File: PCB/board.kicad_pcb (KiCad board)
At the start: 2 copper layers, 161 parts, among them J1 Micro_SD_Card, J10 Conn_01x10, J11 Conn_01x02, J12 Conn_02x04_Odd_Even, J13 Conn_01x02, J14 Conn_01x02, J15 Conn_01x03, J16 Conn_01x02, J17 Conn_01x05, J18 Conn_01x04, J19 Conn_01x04, J2 Conn_ARM_JTAG_SWD_10, J20 Conn_01x02, J21 Conn_01x03, J22 Conn_02x04_Odd_Even, J23 Conn_01x04, J24 Conn_01x04, J25 Conn_01x02, J26 Conn_01x03, J27 Conn_02x04_Odd_Even, J28 Conn_01x04, J29 Conn_01x04, J3 USB_C_Receptacle_USB2.0_14P, J30 Conn_01x02, J31 Conn_01x03, J32 Conn_01x02, J33 Conn_01x02, J34 Conn_01x02, J35 Conn_01x02, J36 Conn_01x02, J37 Conn_01x02, J4 Conn_01x04, J5 Conn_01x04, J6 Conn_01x02, J7 Conn_01x03, J8 Conn_02x04_Odd_Even, J9 Conn_01x10, Q1 IRLML6402, Q2 NMOS, Q3 NMOS, Q4 NMOS, Q5 STP55NF06L, Q6 STP55NF06L, SW1 SW_Push, SW2 SW_Push, U1 STM32H743VITx, U2 AP7361C, U4 TMC Stepstick, U5 TMC Stepstick, U6 TMC Stepstick, U7 TMC Stepstick, U8 AP63203WU, Y2 25 MHz

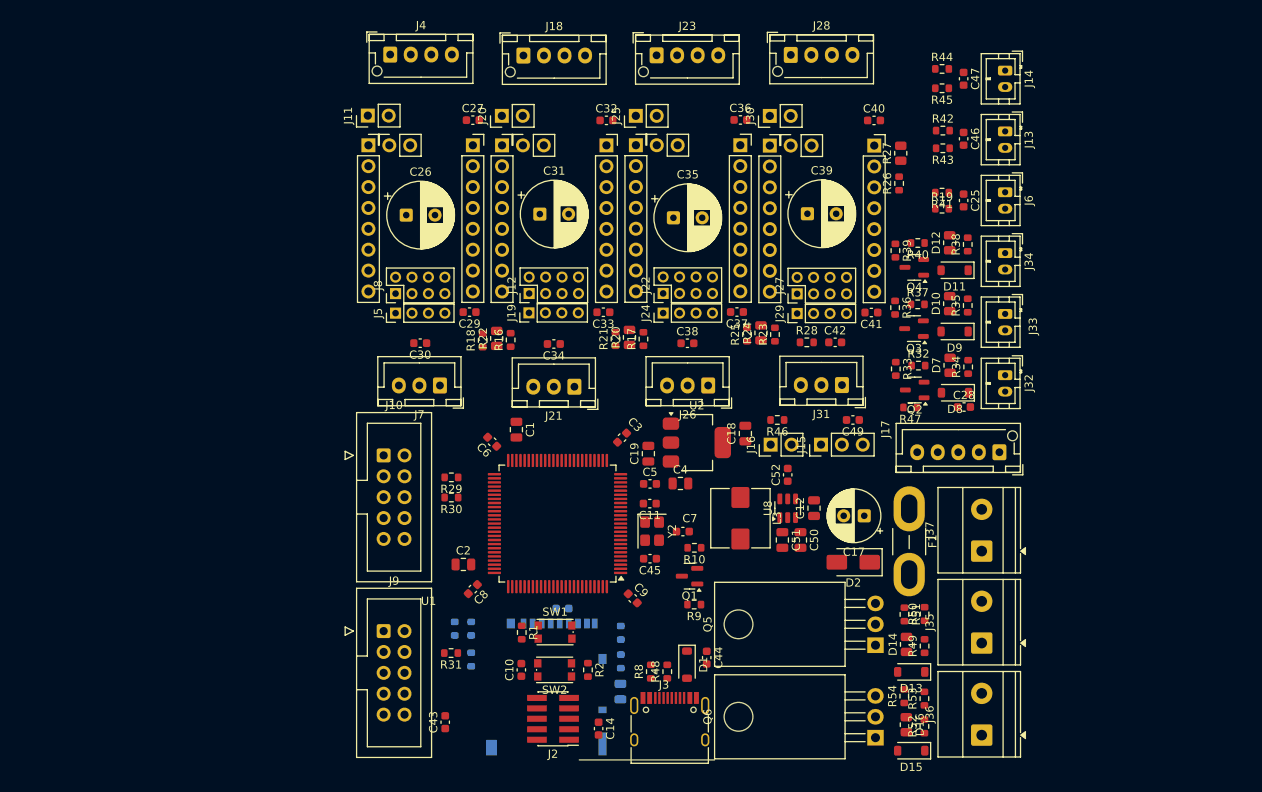
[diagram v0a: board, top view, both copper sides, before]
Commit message: fixed the mosfets on the heaters
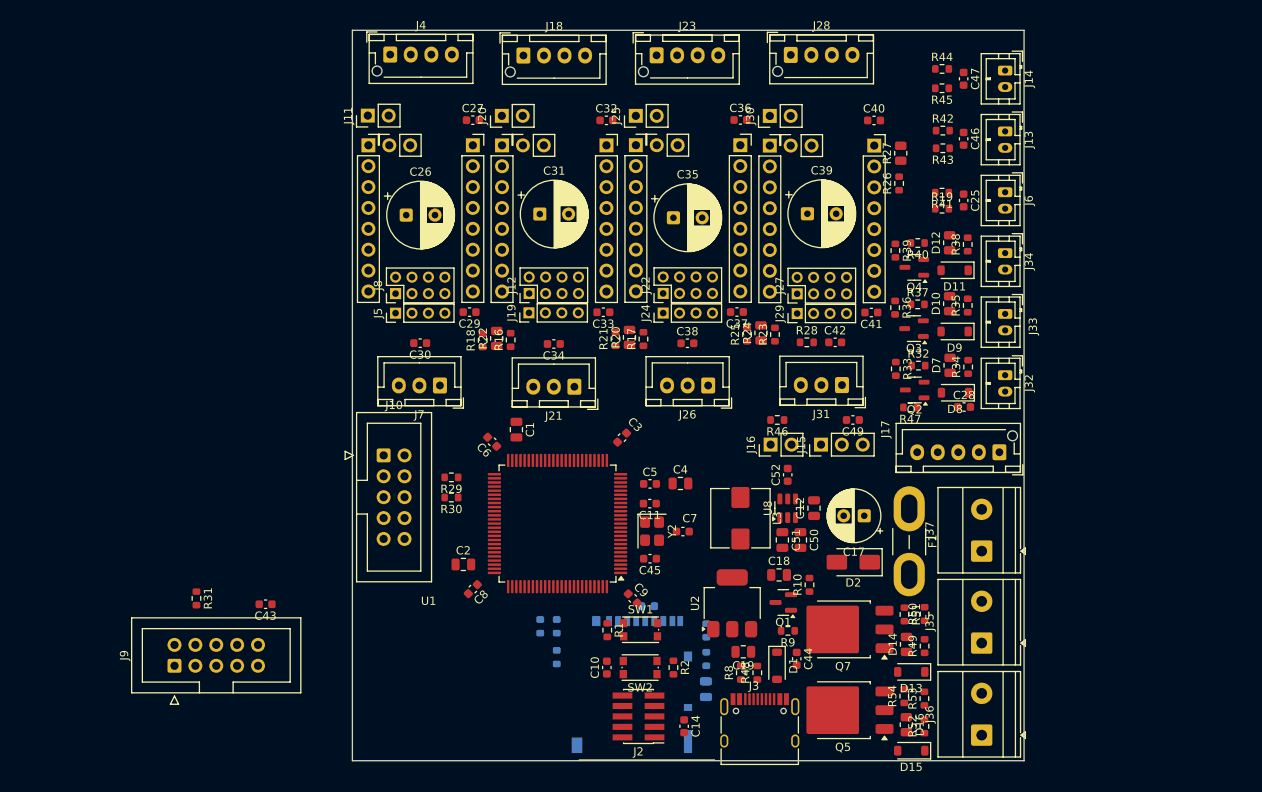
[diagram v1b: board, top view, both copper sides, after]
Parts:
- removed Q6: STP55NF06L, Package_TO_SOT_THT:TO-220-3_Horizontal_TabDown
- added Q7: Q_NMOS_GDS, Package_TO_SOT_SMD:TO-252-3_TabPin2, F.Cu at (213.2, 96.8)
- Q5: value STP55NF06L -> Q_NMOS_GDS; footprint Package_TO_SOT_THT:TO-220-3_Horizontal_TabDown -> Package_TO_SOT_SMD:TO-252-3_TabPin2
- moved R31 31.7 mm to (134.6, 93.0), turned to -90 degrees
- moved C19 26.7 mm to (201.1, 99.5), turned to 180 degrees
- moved C43 26.1 mm to (143.0, 93.8), turned to 180 degrees
- moved J9 25.8 mm to (131.9, 101.2), turned to 90 degrees
- moved U2 20.0 mm to (199.8, 93.7), turned to 90 degrees
- moved C18 17.7 mm to (205.4, 90.2), turned to 0 degrees
- moved R10 14.7 mm to (209.2, 91.4), turned to 90 degrees
- moved Q1 11.8 mm to (206.0, 93.5)
- moved R9 11.8 mm to (206.5, 97.0)
- moved R48 11.0 mm to (202.8, 102.1)
- moved R8 11.0 mm to (200.8, 102.1)
- moved C44 11.0 mm to (207.6, 100.4)
- moved D1 11.0 mm to (205.2, 101.2)
- moved J3 11.0 mm to (203.1, 109.3)
- moved C10 10.4 mm to (184.5, 101.5)
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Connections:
- Q5 pad 1: Net-(D13-A) -> Net-(Q5-G)
- Q5 pad 2: Net-(Q5-G) -> Net-(D13-A)
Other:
- board outline added: 81.7 x 88.8 mm

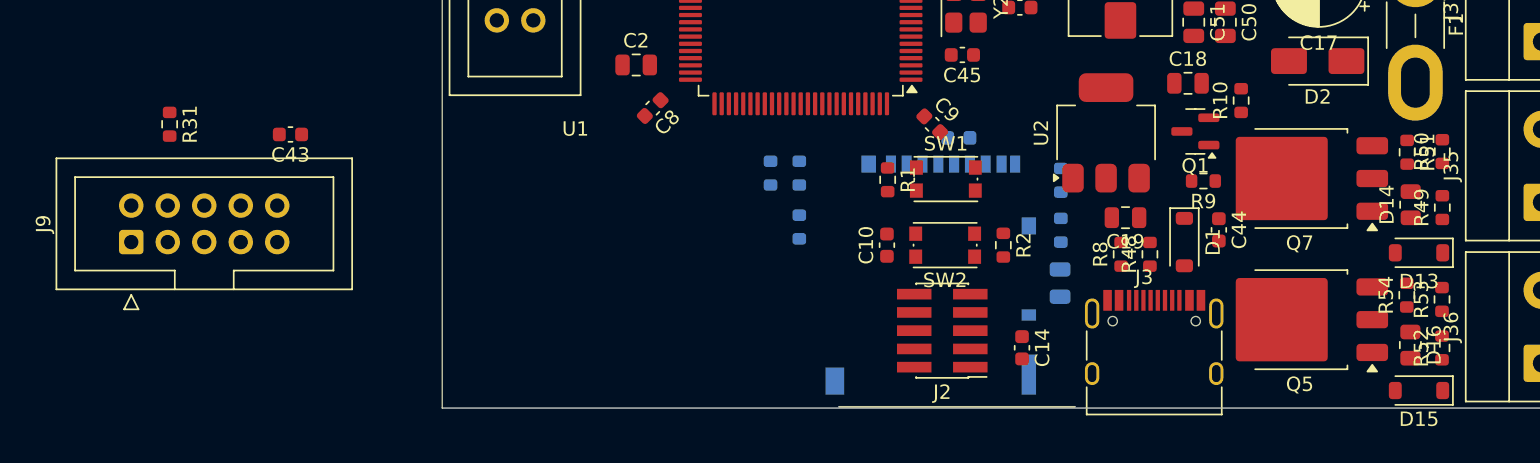
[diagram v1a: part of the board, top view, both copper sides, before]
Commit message: added mounting holes
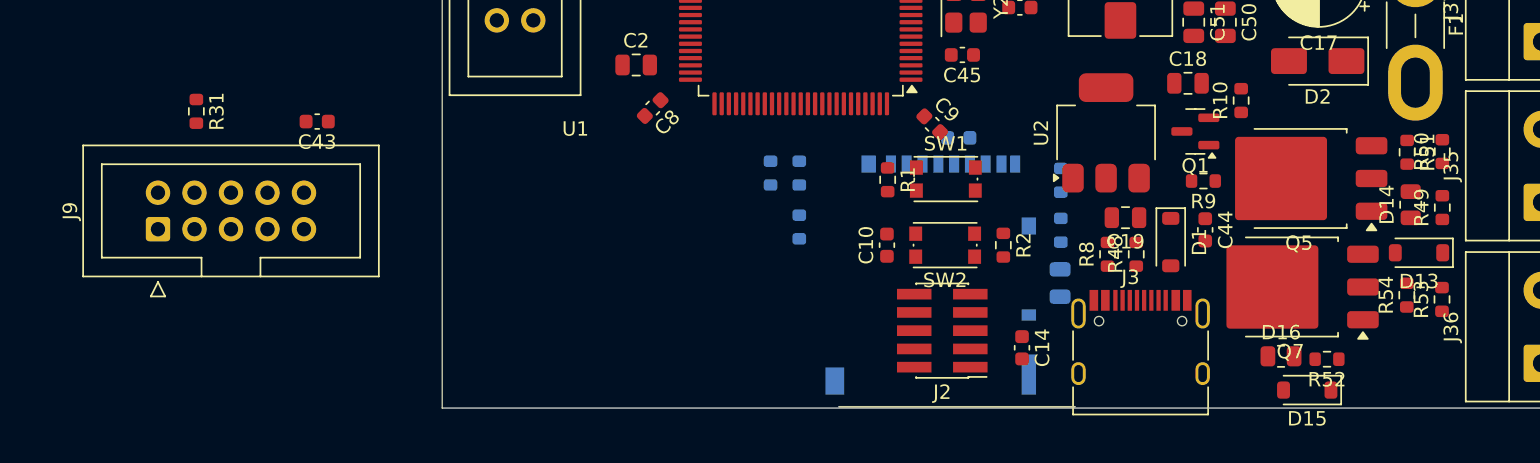
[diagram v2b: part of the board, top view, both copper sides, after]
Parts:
- moved Q5 9.83 mm to (213.2, 96.8)
- moved D16 9.04 mm to (211.9, 109.2), turned to 0 degrees
- moved R52 8.04 mm to (215.1, 109.4), turned to 180 degrees
- moved D15 7.78 mm to (213.8, 111.5)
- moved Q7 7.58 mm to (212.6, 104.4)
- moved J9 2.07 mm to (133.8, 100.4)
- moved C43 2.07 mm to (144.8, 92.9)
- moved R31 2.07 mm to (136.4, 92.2)
- moved R48 0.95 mm to (201.8, 102.1)
- moved R8 0.95 mm to (199.8, 102.1)
- moved C44 0.95 mm to (206.7, 100.4)
- moved D1 0.95 mm to (204.2, 101.2)
- moved J3 0.95 mm to (202.2, 109.3)
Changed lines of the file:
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@@
 	(footprint "Package_TO_SOT_SMD:TO-252-3_TabPin2"
 		(layer "F.Cu")
-		(at 213.235 96.825 180)
+		(at 212.585 104.375 180)
 		(descr "TO-252/DPAK SMD package, http://www.infineon.com/cms/en/product/packages/PG-TO252/PG-TO252-3-1/")
 		(tags "DPAK TO-252 DPAK-3 TO-252-3 SOT-428")
@@
 	(footprint "Capacitor_SMD:C_0603_1608Metric"
 		(layer "F.Cu")
-		(at 142.99 93.76 180)
+		(at 144.85 92.8625 180)
 		(descr "Capacitor SMD 0603 (1608 Metric), square (rectangular) end terminal, IPC-7351 nominal, (Body size source: IPC-SM-782 page 76, https://www.pcb-3d.com/wordpress/wp-content/uploads/ipc-sm-782a_amendment_1_and_2.pdf), generated with kicad-footprint-generator")
 		(tags "capacitor")
@@
 	(footprint "Diode_SMD:D_SOD-123"
 		(layer "F.Cu")
-		(at 205.2 101.25 -90)
+		(at 204.25 101.25 -90)
 		(descr "SOD-123")
 		(tags "SOD-123")
@@
 	(footprint "Resistor_SMD:R_0805_2012Metric"
 		(layer "F.Cu")
-		(at 220.9275 108.4175 -90)
+		(at 211.925 109.2)
 		(descr "Resistor SMD 0805 (2012 Metric), square (rectangular) end terminal, IPC-7351 nominal, (Body size source: IPC-SM-782 page 72, https://www.pcb-3d.com/wordpress/wp-content/uploads/ipc-sm-782a_amendment_1_and_2.pdf), generated with kicad-footprint-generator")
 		(tags "resistor")
 		(property "Reference" "D16"
-			(at 0 -1.65 90)
+			(at 0 -1.65 0)
 			(layer "F.SilkS")
 			(effects
@@
 		)
 		(property "Value" "Green"
-			(at 0 1.65 90)
+			(at 0 1.65 0)
 			(layer "F.Fab")
 			(effects
@@
 		)
 		(property "Datasheet" "~"
-			(at 0 0 90)
+			(at 0 0 0)
 			(layer "F.Fab")
 			(hide yes)
@@
 		)
 		(property "Description" "Light emitting diode"
-			(at 0 0 90)
+			(at 0 0 0)
 			(layer "F.Fab")
 			(hide yes)
@@
 		)
 		(property "Sim.Pins" "1=K 2=A"
-			(at 0 0 270)
+			(at 0 0 0)
 			(unlocked yes)
 			(layer "F.Fab")
@@
 		(attr smd)
 		(fp_line
-			(start -0.227064 0.735)
-			(end 0.227064 0.735)
+			(start -0.227064 -0.735)
+			(end 0.227064 -0.735)
 			(stroke
 				(width 0.12)
@@
 		)
 		(fp_line
-			(start -0.227064 -0.735)
-			(end 0.227064 -0.735)
+			(start -0.227064 0.735)
+			(end 0.227064 0.735)
 			(stroke
 				(width 0.12)
@@
 		)
 		(fp_line
-			(start -1.68 0.95)
-			(end -1.68 -0.95)
+			(start -1.68 -0.95)
+			(end 1.68 -0.95)
 			(stroke
 				(width 0.05)
@@
 		)
 		(fp_line
-			(start 1.68 0.95)
-			(end -1.68 0.95)
+			(start -1.68 0.95)
+			(end -1.68 -0.95)
 			(stroke
 				(width 0.05)
@@
 		)
 		(fp_line
-			(start -1.68 -0.95)
-			(end 1.68 -0.95)
+			(start 1.68 -0.95)
+			(end 1.68 0.95)
 			(stroke
 				(width 0.05)
@@
 		)
 		(fp_line
-			(start 1.68 -0.95)
-			(end 1.68 0.95)
+			(start 1.68 0.95)
+			(end -1.68 0.95)
 			(stroke
 				(width 0.05)
@@
 		)
 		(fp_line
-			(start -1 0.625)
-			(end -1 -0.625)
+			(start -1 -0.625)
+			(end 1 -0.625)
 			(stroke
 				(width 0.1)
@@
 		)
 		(fp_line
-			(start 1 0.625)
-			(end -1 0.625)
+			(start -1 0.625)
+			(end -1 -0.625)
 			(stroke
 				(width 0.1)
@@
 		)
 		(fp_line
-			(start -1 -0.625)
-			(end 1 -0.625)
+			(start 1 -0.625)
+			(end 1 0.625)
 			(stroke
 				(width 0.1)
@@
 		)
 		(fp_line
-			(start 1 -0.625)
-			(end 1 0.625)
+			(start 1 0.625)
+			(end -1 0.625)
 			(stroke
 				(width 0.1)
@@
 		)
 		(fp_text user "${REFERENCE}"
-			(at 0 0 90)
+			(at 0 0 0)
 			(layer "F.Fab")
 			(effects
@@
 		)
 		(pad "1" smd roundrect
-			(at -0.9125 0 270)
+			(at -0.9125 0)
 			(size 1.025 1.4)
 			(layers "F.Cu" "F.Mask" "F.Paste")
@@
 		)
 		(pad "2" smd roundrect
-			(at 0.9125 0 270)
+			(at 0.9125 0)
 			(size 1.025 1.4)
 			(layers "F.Cu" "F.Mask" "F.Paste")
@@
 	(footprint "Resistor_SMD:R_0603_1608Metric"
 		(layer "F.Cu")
-		(at 202.8 102.1 90)
+		(at 201.85 102.1 90)
 		(descr "Resistor SMD 0603 (1608 Metric), square (rectangular) end terminal, IPC-7351 nominal, (Body size source: IPC-SM-782 page 72, https://www.pcb-3d.com/wordpress/wp-content/uploads/ipc-sm-782a_amendment_1_and_2.pdf), generated with kicad-footprint-generator")
 		(tags "resistor")
@@
 	(footprint "Resistor_SMD:R_0603_1608Metric"
 		(layer "F.Cu")
-		(at 200.8 102.1 90)
+		(at 199.85 102.1 90)
 		(descr "Resistor SMD 0603 (1608 Metric), square (rectangular) end terminal, IPC-7351 nominal, (Body size source: IPC-SM-782 page 72, https://www.pcb-3d.com/wordpress/wp-content/uploads/ipc-sm-782a_amendment_1_and_2.pdf), generated with kicad-footprint-generator")
 		(tags "resistor")
@@
 	(footprint "Resistor_SMD:R_0603_1608Metric"
 		(layer "F.Cu")
-		(at 134.58 93.05 -90)
+		(at 136.44 92.1525 -90)
 		(descr "Resistor SMD 0603 (1608 Metric), square (rectangular) end terminal, IPC-7351 nominal, (Body size source: IPC-SM-782 page 72, https://www.pcb-3d.com/wordpress/wp-content/uploads/ipc-sm-782a_amendment_1_and_2.pdf), generated with kicad-footprint-generator")
 		(tags "resistor")
@@
 	(footprint "Connector_USB:USB_C_Receptacle_HRO_TYPE-C-31-M-12"
 		(layer "F.Cu")
-		(at 203.1 109.35)
+		(at 202.15 109.35)
 		(descr "USB Type-C receptacle for USB 2.0 and PD, http://www.krhro.com/uploads/soft/180320/1-1P320120243.pdf")
 		(tags "usb usb-c 2.0 pd")
@@
 	(footprint "Diode_SMD:D_SOD-123"
 		(layer "F.Cu")
-		(at 221.5275 111.58 180)
+		(at 213.75 111.55 180)
 		(descr "SOD-123")
 		(tags "SOD-123")
@@
 	(footprint "Package_TO_SOT_SMD:TO-252-3_TabPin2"
 		(layer "F.Cu")
-		(at 213.235 106.65 180)
+		(at 213.185 96.825 180)
 		(descr "TO-252/DPAK SMD package, http://www.infineon.com/cms/en/product/packages/PG-TO252/PG-TO252-3-1/")
 		(tags "DPAK TO-252 DPAK-3 TO-252-3 SOT-428")
@@
 	(footprint "Resistor_SMD:R_0603_1608Metric"
 		(layer "F.Cu")
-		(at 223.1275 108.6175 90)
+		(at 215.125 109.4 180)
 		(descr "Resistor SMD 0603 (1608 Metric), square (rectangular) end terminal, IPC-7351 nominal, (Body size source: IPC-SM-782 page 72, https://www.pcb-3d.com/wordpress/wp-content/uploads/ipc-sm-782a_amendment_1_and_2.pdf), generated with kicad-footprint-generator")
 		(tags "resistor")
 		(property "Reference" "R52"
-			(at 0 -1.43 90)
+			(at 0 -1.43 0)
 			(layer "F.SilkS")
 			(effects
@@
 		)
 		(property "Value" "4.7K"
-			(at 0 1.43 90)
+			(at 0 1.43 0)
 			(layer "F.Fab")
 			(effects
@@
 		)
 		(property "Datasheet" "~"
-			(at 0 0 90)
+			(at 0 0 0)
 			(layer "F.Fab")
 			(hide yes)
@@
 		)
 		(property "Description" "Resistor"
-			(at 0 0 90)
+			(at 0 0 0)
 			(layer "F.Fab")
 			(hide yes)
@@
 		(attr smd)
 		(fp_line
-			(start -0.237258 -0.5225)
-			(end 0.237258 -0.5225)
+			(start -0.237258 0.5225)
+			(end 0.237258 0.5225)
 			(stroke
 				(width 0.12)
@@
 		)
 		(fp_line
-			(start -0.237258 0.5225)
-			(end 0.237258 0.5225)
+			(start -0.237258 -0.5225)
+			(end 0.237258 -0.5225)
 			(stroke
 				(width 0.12)
@@
 		)
 		(fp_line
-			(start 1.48 -0.73)
-			(end 1.48 0.73)
+			(start 1.48 0.73)
+			(end -1.48 0.73)
 			(stroke
 				(width 0.05)
@@
 		)
 		(fp_line
-			(start -1.48 -0.73)
-			(end 1.48 -0.73)
+			(start 1.48 -0.73)
+			(end 1.48 0.73)
 			(stroke
 				(width 0.05)
@@
 		)
 		(fp_line
-			(start 1.48 0.73)
-			(end -1.48 0.73)
+			(start -1.48 0.73)
+			(end -1.48 -0.73)
 			(stroke
 				(width 0.05)
@@
 		)
 		(fp_line
-			(start -1.48 0.73)
-			(end -1.48 -0.73)
+			(start -1.48 -0.73)
+			(end 1.48 -0.73)
 			(stroke
 				(width 0.05)
@@
 		)
 		(fp_line
-			(start 0.8 -0.4125)
-			(end 0.8 0.4125)
+			(start 0.8 0.4125)
+			(end -0.8 0.4125)
 			(stroke
 				(width 0.1)
@@
 		)
 		(fp_line
-			(start -0.8 -0.4125)
-			(end 0.8 -0.4125)
+			(start 0.8 -0.4125)
+			(end 0.8 0.4125)
 			(stroke
 				(width 0.1)
@@
 		)
 		(fp_line
-			(start 0.8 0.4125)
-			(end -0.8 0.4125)
+			(start -0.8 0.4125)
+			(end -0.8 -0.4125)
 			(stroke
 				(width 0.1)
@@
 		)
 		(fp_line
-			(start -0.8 0.4125)
-			(end -0.8 -0.4125)
+			(start -0.8 -0.4125)
+			(end 0.8 -0.4125)
 			(stroke
 				(width 0.1)
@@
 		)
 		(fp_text user "${REFERENCE}"
-			(at 0 0 90)
+			(at 0 0 0)
 			(layer "F.Fab")
 			(effects
@@
 		)
 		(pad "1" smd roundrect
-			(at -0.825 0 90)
+			(at -0.825 0 180)
 			(size 0.8 0.95)
 			(layers "F.Cu" "F.Mask" "F.Paste")
@@
 		)
 		(pad "2" smd roundrect
-			(at 0.825 0 90)
+			(at 0.825 0 180)
 			(size 0.8 0.95)
 			(layers "F.Cu" "F.Mask" "F.Paste")
@@
 	(footprint "Connector_IDC:IDC-Header_2x05_P2.54mm_Vertical"
 		(layer "F.Cu")
-		(at 131.91 101.25 90)
+		(at 133.77 100.3525 90)
 		(descr "Through hole IDC box header, 2x05, 2.54mm pitch, DIN 41651 / IEC 60603-13, double rows, https://docs.google.com/spreadsheets/d/16SsEcesNF15N3Lb4niX7dcUr-NY5_MFPQhobNuNppn4/edit#gid=0")
 		(tags "Through hole vertical IDC box header THT 2x05 2.54mm double row")
@@
 	(footprint "Capacitor_SMD:C_0603_1608Metric"
 		(layer "F.Cu")
-		(at 207.6 100.4 -90)
+		(at 206.65 100.4 -90)
 		(descr "Capacitor SMD 0603 (1608 Metric), square (rectangular) end terminal, IPC-7351 nominal, (Body size source: IPC-SM-782 page 76, https://www.pcb-3d.com/wordpress/wp-content/uploads/ipc-sm-782a_amendment_1_and_2.pdf), generated with kicad-footprint-generator")
 		(tags "capacitor")
